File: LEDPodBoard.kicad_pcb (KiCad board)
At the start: 2 copper layers, 50.8 x 50.8 mm, 10 parts

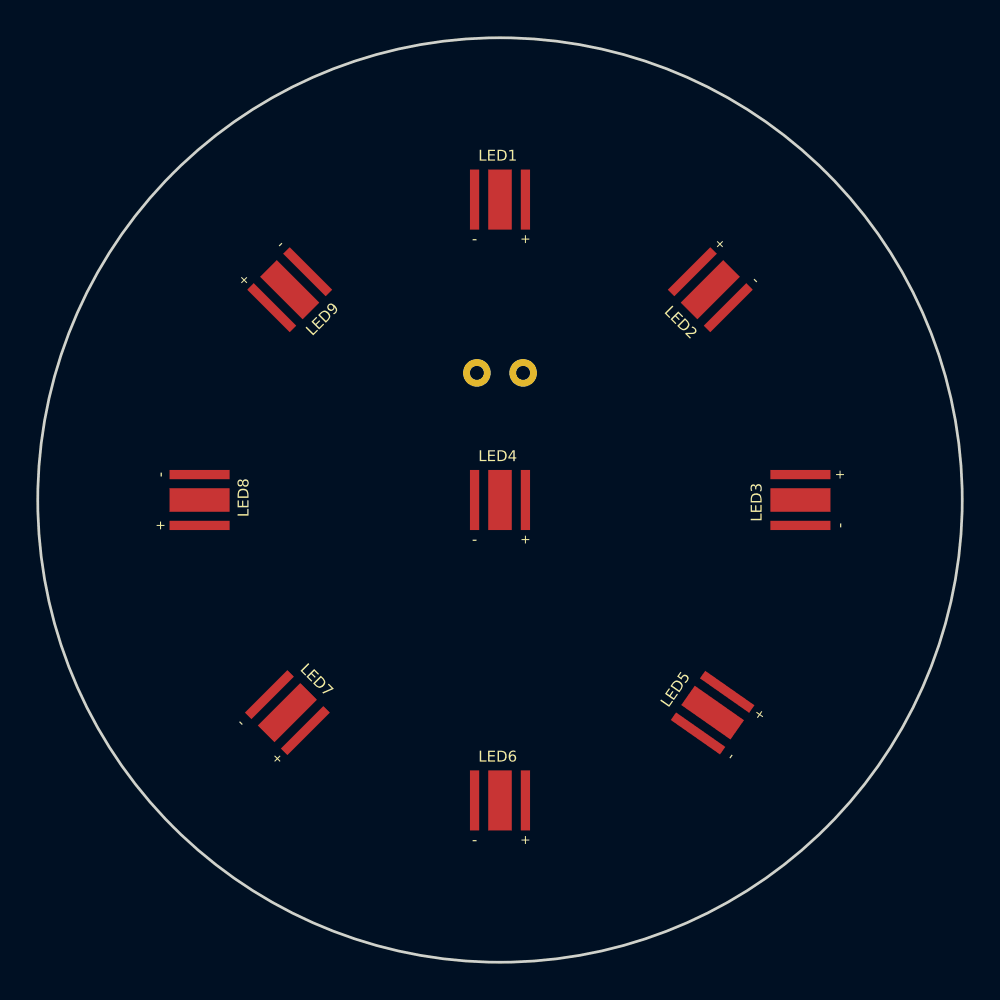
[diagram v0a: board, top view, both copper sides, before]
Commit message: Routed and added silkscreen
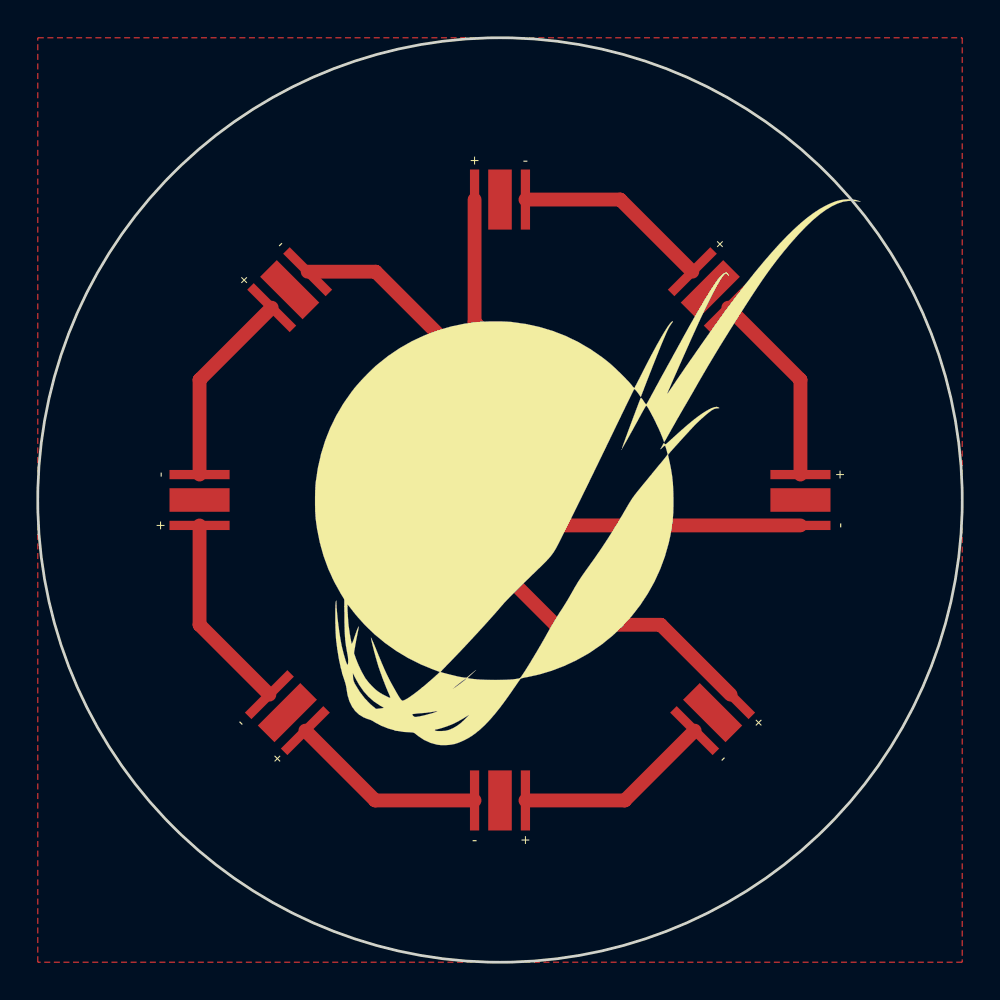
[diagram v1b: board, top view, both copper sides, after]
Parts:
- added G***: LOGO, MRDT_Silkscreens:MRDT_Retro_Logo_40mmX25.3mm, B.Cu at (126.2, 83.1)
- added G***: LOGO, MRDT_Silkscreens:MRDT_Logo_30mm, F.Cu at (131.8, 74.7)
- turned LED1 to 0 degrees
- turned LED5 to 225 degrees
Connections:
- net Net-(LED1-Pad3) renamed /Heat_Slug
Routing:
- net Net-(LED4-Pad2): track 0.00 -> 19.9 mm
- net Net-(LED3-Pad2): track 0.00 -> 16.5 mm
- net /GND: track 0.00 -> 11.6 mm
- net Net-(LED7-Pad2): track 0.00 -> 10.9 mm
- net Net-(LED5-Pad2): track 0.00 -> 10.9 mm
- net Net-(LED6-Pad2): track 0.00 -> 10.9 mm
- net Net-(LED1-Pad2): track 0.00 -> 10.8 mm
- net Net-(LED8-Pad2): track 0.00 -> 10.8 mm
- net Net-(LED2-Pad2): track 0.00 -> 10.8 mm
- net /VIN: track 0.00 -> 10.6 mm
- added copper zone on F.Cu, net /Heat_Slug
